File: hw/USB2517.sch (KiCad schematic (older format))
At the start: 45 parts, among them J1 EXT_PWR, J2 USB_C_Receptacle_USB2.0, U1 MIC5219-3.3, U2 LM1085-5.0, U3 USB2517, U4 24LC02, Y1 24Mhz

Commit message: More placement, more issues
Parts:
- R0: value 0R -> DNP
- R12: value 10k -> DNP
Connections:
- net CFG_SEL2: now reaches R10.2, R11.2, U3.13 (CFG_SEL2)
- net CFG_SEL1: now reaches R8.2, R9.2, U3.42 (HS_IND/CFG_SEL1)
- net VBUS_DET: now reaches R2.1, R3.2, U3.44 (VBUS_DET)
- net USBUP_D-: now reaches J2.A7 (D-), J2.B7 (D-), U3.58 (USBUP_D-)
- net USBUP_D+: now reaches J2.A6 (D+), J2.B6 (D+), U3.59 (USBUP_D+)
- net XTAL2: now reaches C9.1, U3.60 (XTAL2), Y1.1
- net XTAL1: now reaches C10.1, U3.61 (XTAL1), Y1.2
- net RBIAS: now reaches R4.1, U3.63 (RBIAS)
- net 3V3_EN: now reaches R1.1, U1.3 (EN)
- net CC1: now reaches J2.A5 (CC1), R29.2
- net CC2: now reaches J2.B5 (CC2), R30.2
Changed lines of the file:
@@
 P 1550 3750
 F 0 "R0" V 1550 3750 50  0000 C CNN
-F 1 "0R" V 1600 3600 50  0000 C CNN
+F 1 "DNP" V 1600 3600 50  0000 C CNN
 F 2 "Resistor_SMD:R_0603_1608Metric" H 1550 3750 50  0001 C CNN
 F 3 "~" H 1550 3750 50  0001 C CNN
@@
 P 8700 4800
 F 0 "R4" V 8700 4750 50  0000 L CNN
-F 1 "12k 1%" V 8600 4700 50  0000 L CNN
+F 1 "12k 1%" V 8600 4600 50  0000 L CNN
 F 2 "Resistor_SMD:R_0603_1608Metric" H 8700 4800 50  0001 C CNN
 F 3 "~" H 8700 4800 50  0001 C CNN
@@
 P 1550 3400
 F 0 "R12" V 1550 3400 50  0000 C CNN
-F 1 "10k" V 1600 3250 50  0000 C CNN
+F 1 "DNP" V 1600 3250 50  0000 C CNN
 F 2 "Resistor_SMD:R_0603_1608Metric" H 1550 3400 50  0001 C CNN
 F 3 "~" H 1550 3400 50  0001 C CNN
@@
 $EndComp
 Wire Wire Line
-	6300 2900 7050 2900
+	6300 2900 6450 2900
 NoConn ~ 6300 4000
 NoConn ~ 6300 4100
@@
 	5700 4550 5700 4650
 Wire Wire Line
-	1450 2850 1750 2850
-Wire Wire Line
 	1600 3050 1450 3050
-NoConn ~ 1450 2950
 Text Label 1550 2850 1    50   ~ 0
 EXT_PWR
+$Comp
+L power:PWR_FLAG #FLG0103
+U 1 1 5C0990C2
+P 6450 2750
+F 0 "#FLG0103" H 6450 2825 50  0001 C CNN
+F 1 "PWR_FLAG" H 6450 2924 50  0000 C CNN
+F 2 "" H 6450 2750 50  0001 C CNN
+F 3 "~" H 6450 2750 50  0001 C CNN
+	1    6450 2750
+	1    0    0    -1
+$EndComp
+Wire Wire Line
+	6450 2750 6450 2900
+Connection ~ 6450 2900
+Wire Wire Line
+	6450 2900 7050 2900
+$Comp
+L power:PWR_FLAG #FLG0104
+U 1 1 5C0AF8D7
+P 1400 3250
+F 0 "#FLG0104" H 1400 3325 50  0001 C CNN
+F 1 "PWR_FLAG" V 1400 3378 50  0000 L CNN
+F 2 "" H 1400 3250 50  0001 C CNN
+F 3 "~" H 1400 3250 50  0001 C CNN
+	1    1400 3250
+	0    -1   -1   0
+$EndComp
+Wire Wire Line
+	1400 3250 1600 3250
+Connection ~ 1600 3250
+NoConn ~ 1450 2950
+Wire Wire Line
+	1450 2850 1750 2850
+Text Label 1650 4600 3    50   ~ 0
+3V3_EN
+Text Label 7650 4150 3    50   ~ 0
+XTAL1
+Text Label 7650 3850 1    50   ~ 0
+XTAL2
+Text Label 8700 4650 2    50   ~ 0
+RBIAS
+Text Label 9650 3900 0    50   ~ 0
+CFG_SEL1
+Text Label 9650 4000 0    50   ~ 0
+CFG_SEL2
+Text Label 7550 3000 0    50   ~ 0
+VBUS_DET
+Text Label 6300 3100 1    50   ~ 0
+CC1
+Text Label 6300 3200 3    50   ~ 0
+CC2
+Text Label 6300 3600 0    50   ~ 0
+USBUP_D+
+Text Label 6300 3500 0    50   ~ 0
+USBUP_D-
 $EndSCHEMATC

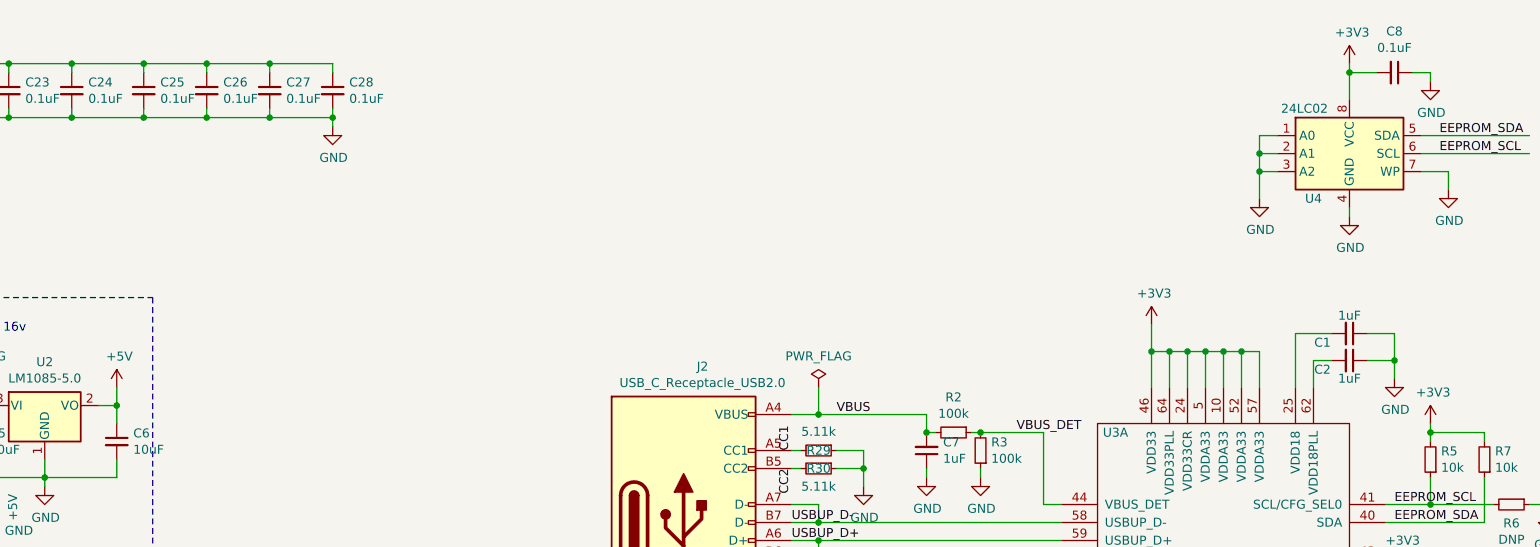
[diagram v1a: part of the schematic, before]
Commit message: More routing, simplification
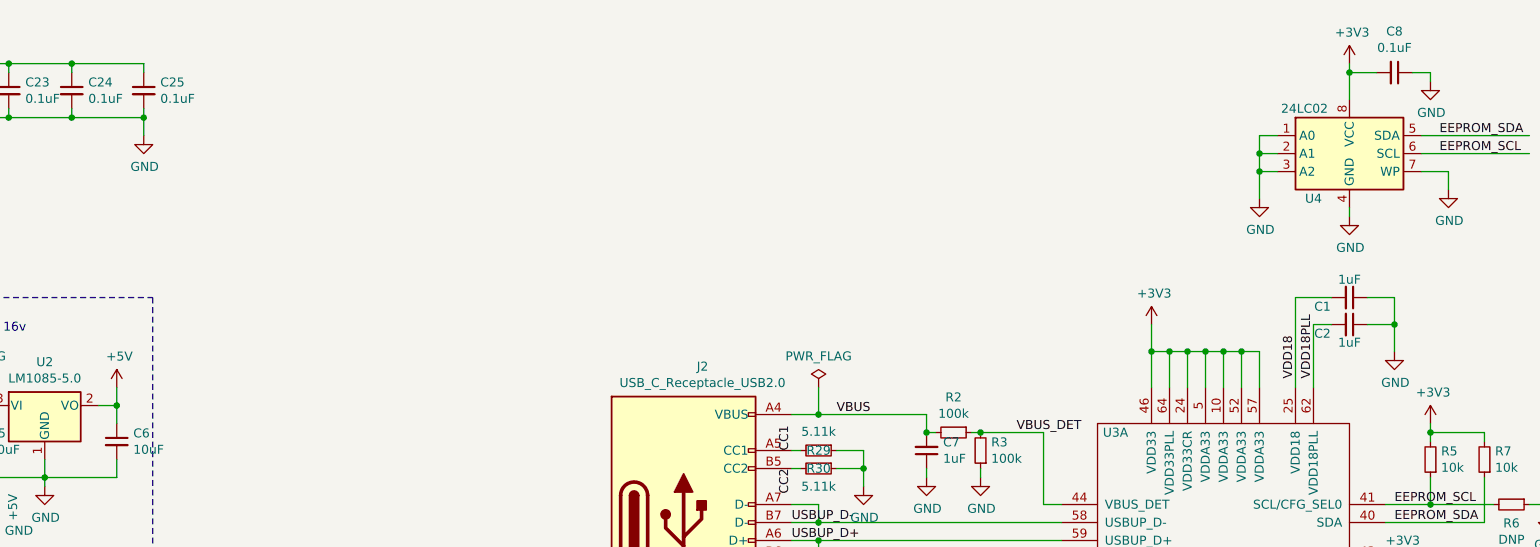
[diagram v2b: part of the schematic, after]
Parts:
- removed C26, C27, C28: 0.1uF, Capacitor_SMD:C_0603_1608Metric, symbol Device:C_Small
- R10, R11, R12, R13, R6, R8, R9: footprint Resistor_SMD:R_0603_1608Metric -> Resistor_SMD:R_0201_0603Metric
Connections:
- net VDD18: now reaches C1.2, U3.25 (VDD18)
- net VDD18PLL: now reaches C2.2, U3.62 (VDD18PLL)
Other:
- moved on the sheet: C1, C2
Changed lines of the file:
@@
 L power:GND #PWR04
 U 1 1 5B958D56
-P 9650 2700
-F 0 "#PWR04" H 9650 2450 50  0001 C CNN
-F 1 "GND" H 9655 2527 50  0000 C CNN
-F 2 "" H 9650 2700 50  0001 C CNN
-F 3 "" H 9650 2700 50  0001 C CNN
-	1    9650 2700
+P 9650 2550
+F 0 "#PWR04" H 9650 2300 50  0001 C CNN
+F 1 "GND" H 9655 2377 50  0000 C CNN
+F 2 "" H 9650 2550 50  0001 C CNN
+F 3 "" H 9650 2550 50  0001 C CNN
+	1    9650 2550
 	1    0    0    -1
 $EndComp
@@
 L Device:C_Small C2
 U 1 1 5B958DE7
-P 9400 2600
-F 0 "C2" V 9450 2450 50  0000 C CNN
-F 1 "1uF" V 9500 2600 50  0000 C CNN
-F 2 "Capacitor_SMD:C_0603_1608Metric" H 9400 2600 50  0001 C CNN
-F 3 "~" H 9400 2600 50  0001 C CNN
-	1    9400 2600
+P 9400 2400
+F 0 "C2" V 9450 2250 50  0000 C CNN
+F 1 "1uF" V 9500 2400 50  0000 C CNN
+F 2 "Capacitor_SMD:C_0603_1608Metric" H 9400 2400 50  0001 C CNN
+F 3 "~" H 9400 2400 50  0001 C CNN
+	1    9400 2400
 	0    1    1    0
 $EndComp
@@
 L Device:C_Small C1
 U 1 1 5B958E1D
-P 9400 2450
-F 0 "C1" V 9450 2300 50  0000 C CNN
-F 1 "1uF" V 9300 2450 50  0000 C CNN
-F 2 "Capacitor_SMD:C_0603_1608Metric" H 9400 2450 50  0001 C CNN
-F 3 "~" H 9400 2450 50  0001 C CNN
-	1    9400 2450
-	0    1    1    0
-$EndComp
-Wire Wire Line
-	9100 2750 9100 2450
-Wire Wire Line
-	9100 2450 9300 2450
-Wire Wire Line
-	9200 2750 9200 2600
-Wire Wire Line
-	9200 2600 9300 2600
-Wire Wire Line
-	9500 2450 9650 2450
-Wire Wire Line
-	9650 2450 9650 2600
-Wire Wire Line
-	9500 2600 9650 2600
-Connection ~ 9650 2600
-Wire Wire Line
-	9650 2600 9650 2700
+P 9400 2250
+F 0 "C1" V 9450 2100 50  0000 C CNN
+F 1 "1uF" V 9300 2250 50  0000 C CNN
+F 2 "Capacitor_SMD:C_0603_1608Metric" H 9400 2250 50  0001 C CNN
+F 3 "~" H 9400 2250 50  0001 C CNN
+	1    9400 2250
+	0    1    1    0
+$EndComp
+Wire Wire Line
+	9100 2750 9100 2250
+Wire Wire Line
+	9100 2250 9300 2250
+Wire Wire Line
+	9200 2750 9200 2400
+Wire Wire Line
+	9200 2400 9300 2400
+Wire Wire Line
+	9500 2250 9650 2250
+Wire Wire Line
+	9650 2250 9650 2400
+Wire Wire Line
+	9500 2400 9650 2400
+Connection ~ 9650 2400
+Wire Wire Line
+	9650 2400 9650 2550
 $Comp
 L power:+3V3 #PWR01
@@
 F 0 "R6" V 10404 3400 50  0000 C CNN
 F 1 "DNP" V 10495 3400 50  0000 C CNN
-F 2 "Resistor_SMD:R_0603_1608Metric" H 10300 3400 50  0001 C CNN
+F 2 "Resistor_SMD:R_0201_0603Metric" H 10300 3400 50  0001 C CNN
 F 3 "~" H 10300 3400 50  0001 C CNN
 	1    10300 3400
@@
 Wire Wire Line
 	9700 3700 9600 3700
-$Comp
-L Device:R_Small R8
-U 1 1 5B9E24F4
-P 10400 3800
-F 0 "R8" V 10400 3800 50  0000 C CNN
-F 1 "DNP" V 10350 3650 50  0000 C CNN
-F 2 "Resistor_SMD:R_0603_1608Metric" H 10400 3800 50  0001 C CNN
-F 3 "~" H 10400 3800 50  0001 C CNN
-	1    10400 3800
-	0    1    1    0
-$EndComp
-$Comp
-L Device:R_Small R9
-U 1 1 5B9E2564
-P 10400 3900
-F 0 "R9" V 10400 3900 50  0000 C CNN
-F 1 "0R" V 10350 3750 50  0000 C CNN
-F 2 "Resistor_SMD:R_0603_1608Metric" H 10400 3900 50  0001 C CNN
-F 3 "~" H 10400 3900 50  0001 C CNN
-	1    10400 3900
-	0    1    1    0
-$EndComp
-$Comp
-L Device:R_Small R10
-U 1 1 5B9E25A0
-P 10400 4000
-F 0 "R10" V 10400 4000 50  0000 C CNN
-F 1 "0R" V 10450 3850 50  0000 C CNN
-F 2 "Resistor_SMD:R_0603_1608Metric" H 10400 4000 50  0001 C CNN
-F 3 "~" H 10400 4000 50  0001 C CNN
-	1    10400 4000
-	0    1    1    0
-$EndComp
-$Comp
-L Device:R_Small R11
-U 1 1 5B9E25DE
-P 10400 4100
-F 0 "R11" V 10400 4100 50  0000 C CNN
-F 1 "DNP" V 10450 3950 50  0000 C CNN
-F 2 "Resistor_SMD:R_0603_1608Metric" H 10400 4100 50  0001 C CNN
-F 3 "~" H 10400 4100 50  0001 C CNN
-	1    10400 4100
-	0    1    1    0
-$EndComp
 Wire Wire Line
 	10200 3900 10200 3800
 Wire Wire Line
-	10200 3800 10300 3800
-Wire Wire Line
-	10300 3900 10200 3900
-Connection ~ 10200 3900
-Wire Wire Line
 	10200 4000 10200 4100
-Wire Wire Line
-	10200 4100 10300 4100
 Connection ~ 10200 4000
 Wire Wire Line
@@
 	0    -1   -1   0
 $EndComp
-Wire Wire Line
-	10600 4000 10500 4000
-Wire Wire Line
-	10600 4100 10500 4100
-Wire Wire Line
-	10600 3900 10500 3900
-Wire Wire Line
-	10600 3800 10500 3800
 $Comp
 L Device:R_Small R7
@@
 F 0 "R12" V 1550 3400 50  0000 C CNN
 F 1 "DNP" V 1600 3250 50  0000 C CNN
-F 2 "Resistor_SMD:R_0603_1608Metric" H 1550 3400 50  0001 C CNN
+F 2 "Resistor_SMD:R_0201_0603Metric" H 1550 3400 50  0001 C CNN
 F 3 "~" H 1550 3400 50  0001 C CNN
 	1    1550 3400
@@
 F 0 "R13" V 1550 3550 50  0000 C CNN
 F 1 "10k" V 1600 3400 50  0000 C CNN
-F 2 "Resistor_SMD:R_0603_1608Metric" H 1550 3550 50  0001 C CNN
+F 2 "Resistor_SMD:R_0201_0603Metric" H 1550 3550 50  0001 C CNN
 F 3 "~" H 1550 3550 50  0001 C CNN
 	1    1550 3550
@@
 L power:GND #PWR063
 U 1 1 5BD83E91
-P 3750 1300
-F 0 "#PWR063" H 3750 1050 50  0001 C CNN
-F 1 "GND" H 3755 1127 50  0000 C CNN
-F 2 "" H 3750 1300 50  0001 C CNN
-F 3 "" H 3750 1300 50  0001 C CNN
-	1    3750 1300
+P 2700 1350
+F 0 "#PWR063" H 2700 1100 50  0001 C CNN
+F 1 "GND" H 2705 1177 50  0000 C CNN
+F 2 "" H 2700 1350 50  0001 C CNN
+F 3 "" H 2700 1350 50  0001 C CNN
+	1    2700 1350
 	1    0    0    -1
 $EndComp
@@
 	1    0    0    -1
 $EndComp
-$Comp
-L Device:C_Small C26
-U 1 1 5BD844B3
-P 3050 1100
-F 0 "C26" H 3142 1146 50  0000 L CNN
-F 1 "0.1uF" H 3142 1055 50  0000 L CNN
-F 2 "Capacitor_SMD:C_0603_1608Metric" H 3050 1100 50  0001 C CNN
-F 3 "~" H 3050 1100 50  0001 C CNN
-	1    3050 1100
-	1    0    0    -1
-$EndComp
-$Comp
-L Device:C_Small C27
-U 1 1 5BD8451F
-P 3400 1100
-F 0 "C27" H 3492 1146 50  0000 L CNN
-F 1 "0.1uF" H 3492 1055 50  0000 L CNN
-F 2 "Capacitor_SMD:C_0603_1608Metric" H 3400 1100 50  0001 C CNN
-F 3 "~" H 3400 1100 50  0001 C CNN
-	1    3400 1100
-	1    0    0    -1
-$EndComp
-$Comp
-L Device:C_Small C28
-U 1 1 5BD8458D
-P 3750 1100
-F 0 "C28" H 3842 1146 50  0000 L CNN
-F 1 "0.1uF" H 3842 1055 50  0000 L CNN
-F 2 "Capacitor_SMD:C_0603_1608Metric" H 3750 1100 50  0001 C CNN
-F 3 "~" H 3750 1100 50  0001 C CNN
-	1    3750 1100
-	1    0    0    -1
-$EndComp
 Wire Wire Line
 	1150 900  1150 950
 Wire Wire Line
 	1150 950  1550 950
-Wire Wire Line
-	3750 950  3750 1000
 Connection ~ 1150 950
 Wire Wire Line
 	1150 950  1150 1000
 Wire Wire Line
-	3400 1000 3400 950
-Connection ~ 3400 950
-Wire Wire Line
-	3400 950  3750 950
-Wire Wire Line
-	3050 1000 3050 950
-Connection ~ 3050 950
-Wire Wire Line
-	3050 950  3400 950
-Wire Wire Line
 	2700 1000 2700 950
-Connection ~ 2700 950
-Wire Wire Line
-	2700 950  3050 950
 Wire Wire Line
 	2300 950  2300 1000
@@
 	1550 950  1950 950
 Wire Wire Line
-	3750 1250 3400 1250
-Wire Wire Line
 	1150 1250 1150 1200
 Wire Wire Line
-	3750 1300 3750 1250
-Connection ~ 3750 1250
-Wire Wire Line
-	3750 1250 3750 1200
-Wire Wire Line
-	3400 1200 3400 1250
-Connection ~ 3400 1250
-Wire Wire Line
-	3400 1250 3050 1250
-Wire Wire Line
-	3050 1200 3050 1250
-Connection ~ 3050 1250
-Wire Wire Line
-	3050 1250 2700 1250
-Wire Wire Line
 	2700 1200 2700 1250
-Connection ~ 2700 1250
 Wire Wire Line
 	2700 1250 2300 1250
@@
 Text Label 6300 3500 0    50   ~ 0
 USBUP_D-
+Wire Wire Line
+	10600 4000 10500 4000
+Wire Wire Line
+	10600 3800 10500 3800
+Wire Wire Line
+	10200 3800 10300 3800
+Wire Wire Line
+	10600 3900 10500 3900
+Connection ~ 10200 3900
+Wire Wire Line
+	10300 3900 10200 3900
+Wire Wire Line
+	10200 4100 10300 4100
+Wire Wire Line
+	10600 4100 10500 4100
+$Comp
+L Device:R_Small R11
+U 1 1 5B9E25DE
+P 10400 4100
+F 0 "R11" V 10400 4100 50  0000 C CNN
+F 1 "DNP" V 10450 3950 50  0000 C CNN
+F 2 "Resistor_SMD:R_0201_0603Metric" H 10400 4100 50  0001 C CNN
+F 3 "~" H 10400 4100 50  0001 C CNN
+	1    10400 4100
+	0    1    1    0
+$EndComp
+$Comp
+L Device:R_Small R10
+U 1 1 5B9E25A0
+P 10400 4000
+F 0 "R10" V 10400 4000 50  0000 C CNN
+F 1 "0R" V 10450 3850 50  0000 C CNN
+F 2 "Resistor_SMD:R_0201_0603Metric" H 10400 4000 50  0001 C CNN
+F 3 "~" H 10400 4000 50  0001 C CNN
+	1    10400 4000
+	0    1    1    0
+$EndComp
+$Comp
+L Device:R_Small R8
+U 1 1 5B9E24F4
+P 10400 3800
+F 0 "R8" V 10400 3800 50  0000 C CNN
+F 1 "DNP" V 10350 3650 50  0000 C CNN
+F 2 "Resistor_SMD:R_0201_0603Metric" H 10400 3800 50  0001 C CNN
+F 3 "~" H 10400 3800 50  0001 C CNN
+	1    10400 3800
+	0    1    1    0
+$EndComp
+$Comp
+L Device:R_Small R9
+U 1 1 5B9E2564
+P 10400 3900
+F 0 "R9" V 10400 3900 50  0000 C CNN
+F 1 "0R" V 10350 3750 50  0000 C CNN
+F 2 "Resistor_SMD:R_0201_0603Metric" H 10400 3900 50  0001 C CNN
+F 3 "~" H 10400 3900 50  0001 C CNN
+	1    10400 3900
+	0    1    1    0
+$EndComp
+Text Label 9200 2700 1    50   ~ 0
+VDD18PLL
+Text Label 9100 2700 1    50   ~ 0
+VDD18
+Wire Wire Line
+	2700 1250 2700 1350
+Connection ~ 2700 1250
 $EndSCHEMATC

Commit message: Final
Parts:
- added TP1: EEPROM_SDA, TestPoint:TestPoint_Pad_D1.0mm, symbol Connector:TestPoint
- added TP2: EEPROM_SCL, TestPoint:TestPoint_Pad_D1.0mm, symbol Connector:TestPoint
- added TP4: VBUS_DET, TestPoint:TestPoint_Pad_D1.0mm, symbol Connector:TestPoint
- added TP5: USB_UP_D-, TestPoint:TestPoint_Pad_D1.0mm, symbol Connector:TestPoint
- added TP6: USBUP_D+, TestPoint:TestPoint_Pad_D1.0mm, symbol Connector:TestPoint
- C8: value 0.1uF -> DNP
- R5, R7: value 10k -> DNP
- R6: value DNP -> 10k; footprint Resistor_SMD:R_0201_0603Metric -> Resistor_SMD:R_0603_1608Metric
- U4: value 24LC02 -> DNP/24LC02
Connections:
- net EEPROM_SCL: now also TP2.1
- net EEPROM_SDA: now also TP1.1
- net USBUP_D+: now also TP6.1
- net USBUP_D-: now also TP5.1
- net VBUS_DET: now also TP4.1
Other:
- note added: "0"
- note added: "1"
- note added: "BUS Powered (Might not work):\nMount R0,R12\nRemove U2, C6, R13\n"
- note added: "CFG0_SEL"
- note added: "CFG1_SEL"
- note added: "CFG2_SEL"
- note added: "Internal default, dynamic power: 0,0,1\nEEPROM: 1,1,0\nFor EEPROM: Mount C8, R5, R7, U4\nRemove R6"
- note added: "R10"
- note added: "R11"
- note added: "R5"
- note added: "R6"
- note added: "R8"
- note added: "R9"
- note added: "Self-powered: Mount U2, C5, C6, R13\nRemove: R0, R13\n"
- note added: "Strap options"
- note removed: "Place either R0 or LM1085"
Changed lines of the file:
@@
 Wire Notes Line
 	2750 2250 2750 4000
-Text Notes 850  2350 0    50   ~ 0
-Place either R0 or LM1085
 Text Notes 850  3950 0    50   ~ 0
 R0 must be able to handle 500mA at least
@@
 	2550 2950 2550 2850
 Connection ~ 2550 2850
-Text Notes 850  2450 0    50   ~ 0
+Text Notes 850  2350 0    50   ~ 0
 C5 should be rated for at least 16v
 $Comp
@@
 P 10300 3400
 F 0 "R6" V 10404 3400 50  0000 C CNN
-F 1 "DNP" V 10495 3400 50  0000 C CNN
-F 2 "Resistor_SMD:R_0201_0603Metric" H 10300 3400 50  0001 C CNN
+F 1 "10k" V 10495 3400 50  0000 C CNN
+F 2 "Resistor_SMD:R_0603_1608Metric" H 10300 3400 50  0001 C CNN
 F 3 "~" H 10300 3400 50  0001 C CNN
 	1    10300 3400
@@
 P 9850 3150
 F 0 "R5" H 9791 3104 50  0000 R CNN
-F 1 "10k" H 9791 3195 50  0000 R CNN
+F 1 "DNP" H 9791 3195 50  0000 R CNN
 F 2 "Resistor_SMD:R_0603_1608Metric" H 9850 3150 50  0001 C CNN
 F 3 "~" H 9850 3150 50  0001 C CNN
@@
 P 10150 3150
 F 0 "R7" H 10091 3104 50  0000 R CNN
-F 1 "10k" H 10091 3195 50  0000 R CNN
+F 1 "DNP" H 10091 3195 50  0000 R CNN
 F 2 "Resistor_SMD:R_0603_1608Metric" H 10150 3150 50  0001 C CNN
 F 3 "~" H 10150 3150 50  0001 C CNN
@@
 P 9400 1450
 F 0 "U4" H 9200 1200 50  0000 C CNN
-F 1 "24LC02" H 9150 1700 50  0000 C CNN
+F 1 "DNP/24LC02" H 9150 1700 50  0000 C CNN
 F 2 "Package_SO:SOIC-8_3.9x4.9mm_P1.27mm" H 9400 1450 50  0001 C CNN
 F 3 "http://ww1.microchip.com/downloads/en/DeviceDoc/21709c.pdf" H 9400 1450 50  0001 C CNN
@@
 L power:GND #PWR016
 U 1 1 5BA4DFC3
-P 9950 1650
-F 0 "#PWR016" H 9950 1400 50  0001 C CNN
-F 1 "GND" H 9955 1477 50  0000 C CNN
-F 2 "" H 9950 1650 50  0001 C CNN
-F 3 "" H 9950 1650 50  0001 C CNN
-	1    9950 1650
-	1    0    0    -1
-$EndComp
-Wire Wire Line
-	9950 1550 9950 1650
-Wire Wire Line
-	9800 1550 9950 1550
+P 10150 1600
+F 0 "#PWR016" H 10150 1350 50  0001 C CNN
+F 1 "GND" H 10155 1427 50  0000 C CNN
+F 2 "" H 10150 1600 50  0001 C CNN
+F 3 "" H 10150 1600 50  0001 C CNN
+	1    10150 1600
+	1    0    0    -1
+$EndComp
 $Comp
 L Device:C_Small C8
@@
 P 9650 1000
 F 0 "C8" V 9421 1000 50  0000 C CNN
-F 1 "0.1uF" V 9512 1000 50  0000 C CNN
+F 1 "DNP" V 9512 1000 50  0000 C CNN
 F 2 "Capacitor_SMD:C_0603_1608Metric" H 9650 1000 50  0001 C CNN
 F 3 "~" H 9650 1000 50  0001 C CNN
@@
 Connection ~ 6450 3500
 Wire Wire Line
-	6450 3500 7800 3500
+	6450 3500 6850 3500
 Wire Wire Line
 	6300 3700 6450 3700
@@
 Connection ~ 6450 3600
 Wire Wire Line
-	6450 3600 7800 3600
+	6450 3600 6850 3600
 $Comp
 L Device:R_Small R29
@@
 	2700 1250 2700 1350
 Connection ~ 2700 1250
+Text Notes 4000 750  0    50   ~ 0
+Strap options
+Text Notes 4000 900  0    50   ~ 0
+CFG0_SEL
+Text Notes 4000 1050 0    50   ~ 0
+CFG1_SEL
+Text Notes 4000 1200 0    50   ~ 0
+CFG2_SEL
+Text Notes 4700 750  0    50   ~ 0
+1
+Text Notes 4900 750  0    50   ~ 0
+0
+Text Notes 4700 1050 0    50   ~ 0
+R8
+Text Notes 4900 1050 0    50   ~ 0
+R9
+Text Notes 4700 1200 0    50   ~ 0
+R10
+Text Notes 4900 1200 0    50   ~ 0
+R11
+Text Notes 4900 900  0    50   ~ 0
+R6
+Text Notes 4700 900  0    50   ~ 0
+R5
+Wire Notes Line
+	3950 650  5100 650
+Wire Notes Line
+	5100 650  5100 1250
+Wire Notes Line
+	5100 1250 3950 1250
+Wire Notes Line
+	3950 1250 3950 650
+Wire Notes Line
+	4600 650  4600 1250
+Wire Notes Line
+	4850 650  4850 1250
+Wire Notes Line
+	3950 800  5100 800
+Wire Notes Line
+	5100 950  3950 950
+Wire Notes Line
+	3950 1100 5100 1100
+Text Notes 3950 1600 0    50   ~ 0
+Internal default, dynamic power: 0,0,1\nEEPROM: 1,1,0\nFor EEPROM: Mount C8, R5, R7, U4\nRemove R6
+Text Notes 850  1900 0    50   ~ 0
+Self-powered: Mount U2, C5, C6, R13\nRemove: R0, R13\n
+Text Notes 850  2150 0    50   ~ 0
+BUS Powered (Might not work):\nMount R0,R12\nRemove U2, C6, R13\n
+$Comp
+L Connector:TestPoint TP1
+U 1 1 5C0DAAB2
+P 10400 1350
+F 0 "TP1" V 10400 1537 50  0000 L CNN
+F 1 "EEPROM_SDA" V 10445 1538 50  0001 L CNN
+F 2 "TestPoint:TestPoint_Pad_D1.0mm" H 10600 1350 50  0001 C CNN
+F 3 "~" H 10600 1350 50  0001 C CNN
+	1    10400 1350
+	0    1    1    0
+$EndComp
+$Comp
+L Connector:TestPoint TP2
+U 1 1 5C0DB81C
+P 10400 1450
+F 0 "TP2" V 10400 1700 50  0000 C CNN
+F 1 "EEPROM_SCL" V 10400 1950 50  0001 C CNN
+F 2 "TestPoint:TestPoint_Pad_D1.0mm" H 10600 1450 50  0001 C CNN
+F 3 "~" H 10600 1450 50  0001 C CNN
+	1    10400 1450
+	0    1    1    0
+$EndComp
+Wire Wire Line
+	10150 1550 10150 1600
+$Comp
+L Connector:TestPoint TP5
+U 1 1 5C12FA8F
+P 6850 3500
+F 0 "TP5" H 6908 3574 50  0000 L CNN
+F 1 "USB_UP_D-" V 6895 3688 50  0001 L CNN
+F 2 "TestPoint:TestPoint_Pad_D1.0mm" H 7050 3500 50  0001 C CNN
+F 3 "~" H 7050 3500 50  0001 C CNN
+	1    6850 3500
+	1    0    0    -1
+$EndComp
+Connection ~ 6850 3500
+Wire Wire Line
+	6850 3500 7800 3500
+$Comp
+L Connector:TestPoint TP6
+U 1 1 5C12FD0C
+P 6850 3600
+F 0 "TP6" H 6792 3673 50  0000 R CNN
+F 1 "USBUP_D+" V 6895 3788 50  0001 L CNN
+F 2 "TestPoint:TestPoint_Pad_D1.0mm" H 7050 3600 50  0001 C CNN
+F 3 "~" H 7050 3600 50  0001 C CNN
+	1    6850 3600
+	-1   0    0    1
+$EndComp
+Connection ~ 6850 3600
+Wire Wire Line
+	6850 3600 7800 3600
+$Comp
+L Connector:TestPoint TP4
+U 1 1 5C1307F5
+P 7350 3000
+F 0 "TP4" H 7408 3074 50  0000 L CNN
+F 1 "VBUS_DET" V 7395 3188 50  0001 L CNN
+F 2 "TestPoint:TestPoint_Pad_D1.0mm" H 7550 3000 50  0001 C CNN
+F 3 "~" H 7550 3000 50  0001 C CNN
+	1    7350 3000
+	1    0    0    -1
+$EndComp
+Wire Wire Line
+	9800 1550 10150 1550
 $EndSCHEMATC
